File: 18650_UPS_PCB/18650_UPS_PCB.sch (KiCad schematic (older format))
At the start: 44 parts, among them J1 USB_B_Micro, J2 Conn_01x02, J3 Conn_01x02, SW1 SW_DIP_x02, U1 STLINK-V3MINI, U10 LR9102G-xx, U11 MP2667, U2 INA237, U3 EA_DOGS104N-A, U5 STM32L151RCTx

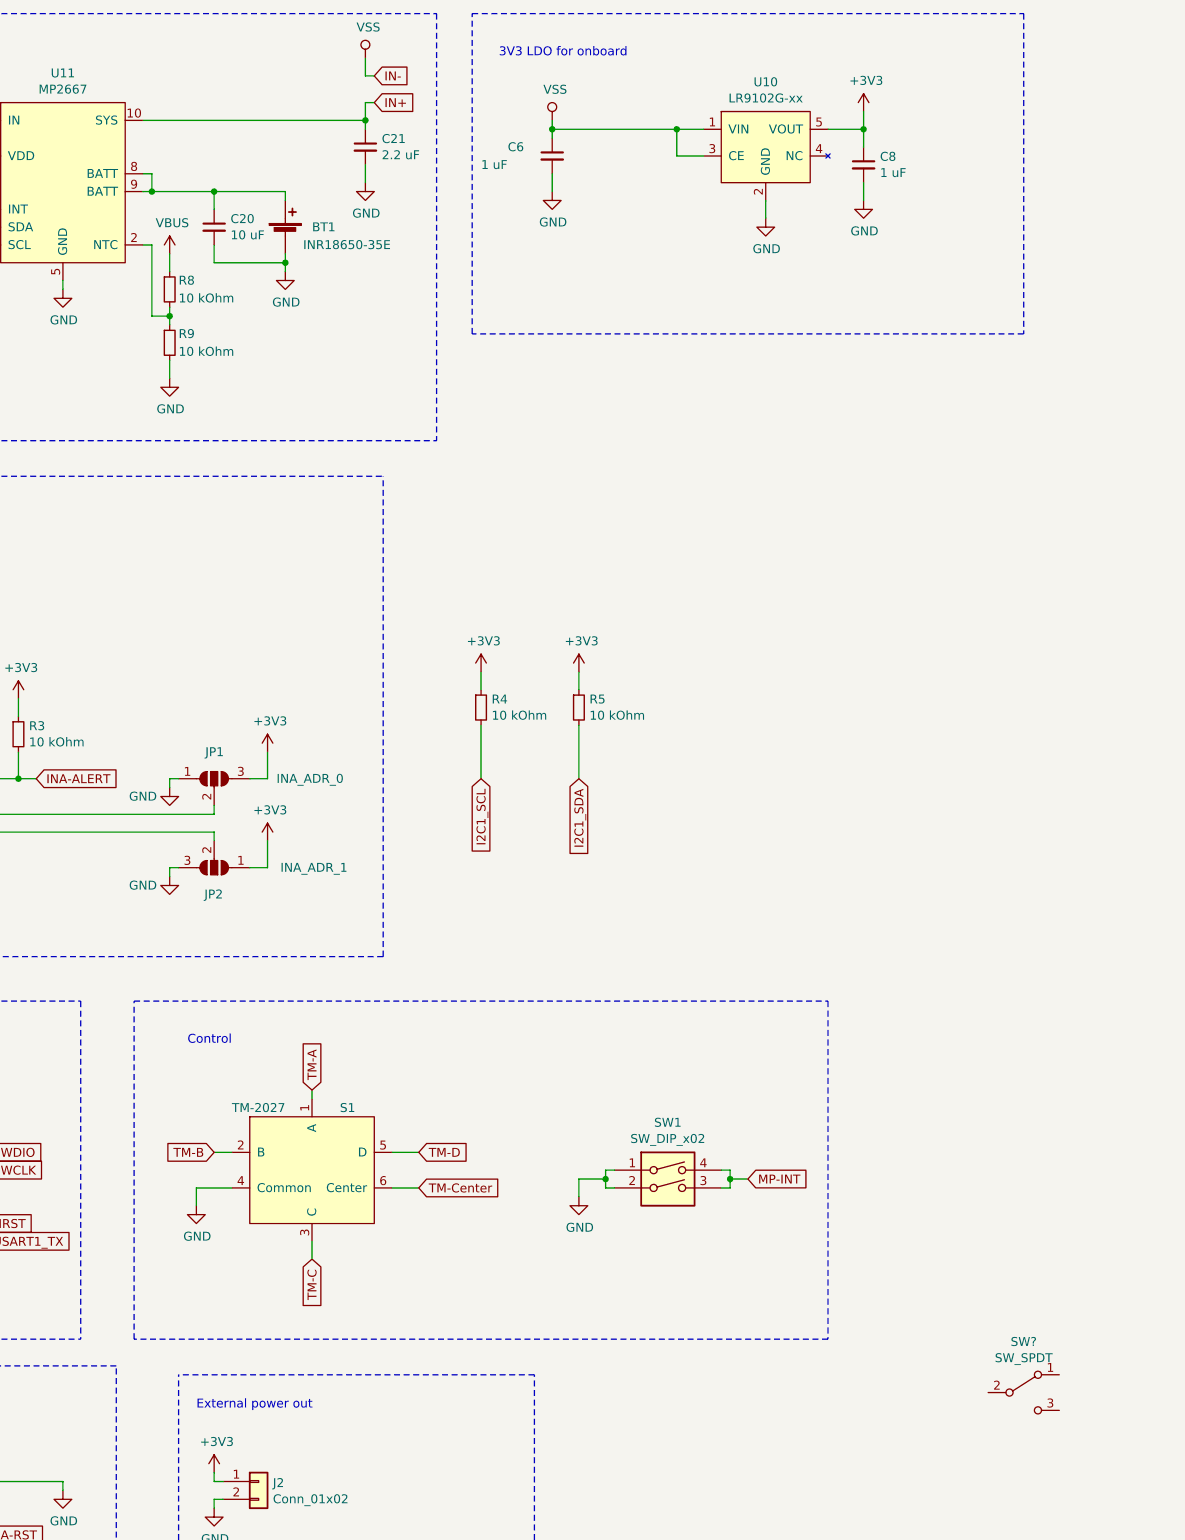
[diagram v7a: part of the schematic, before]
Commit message: added silkscreen markings
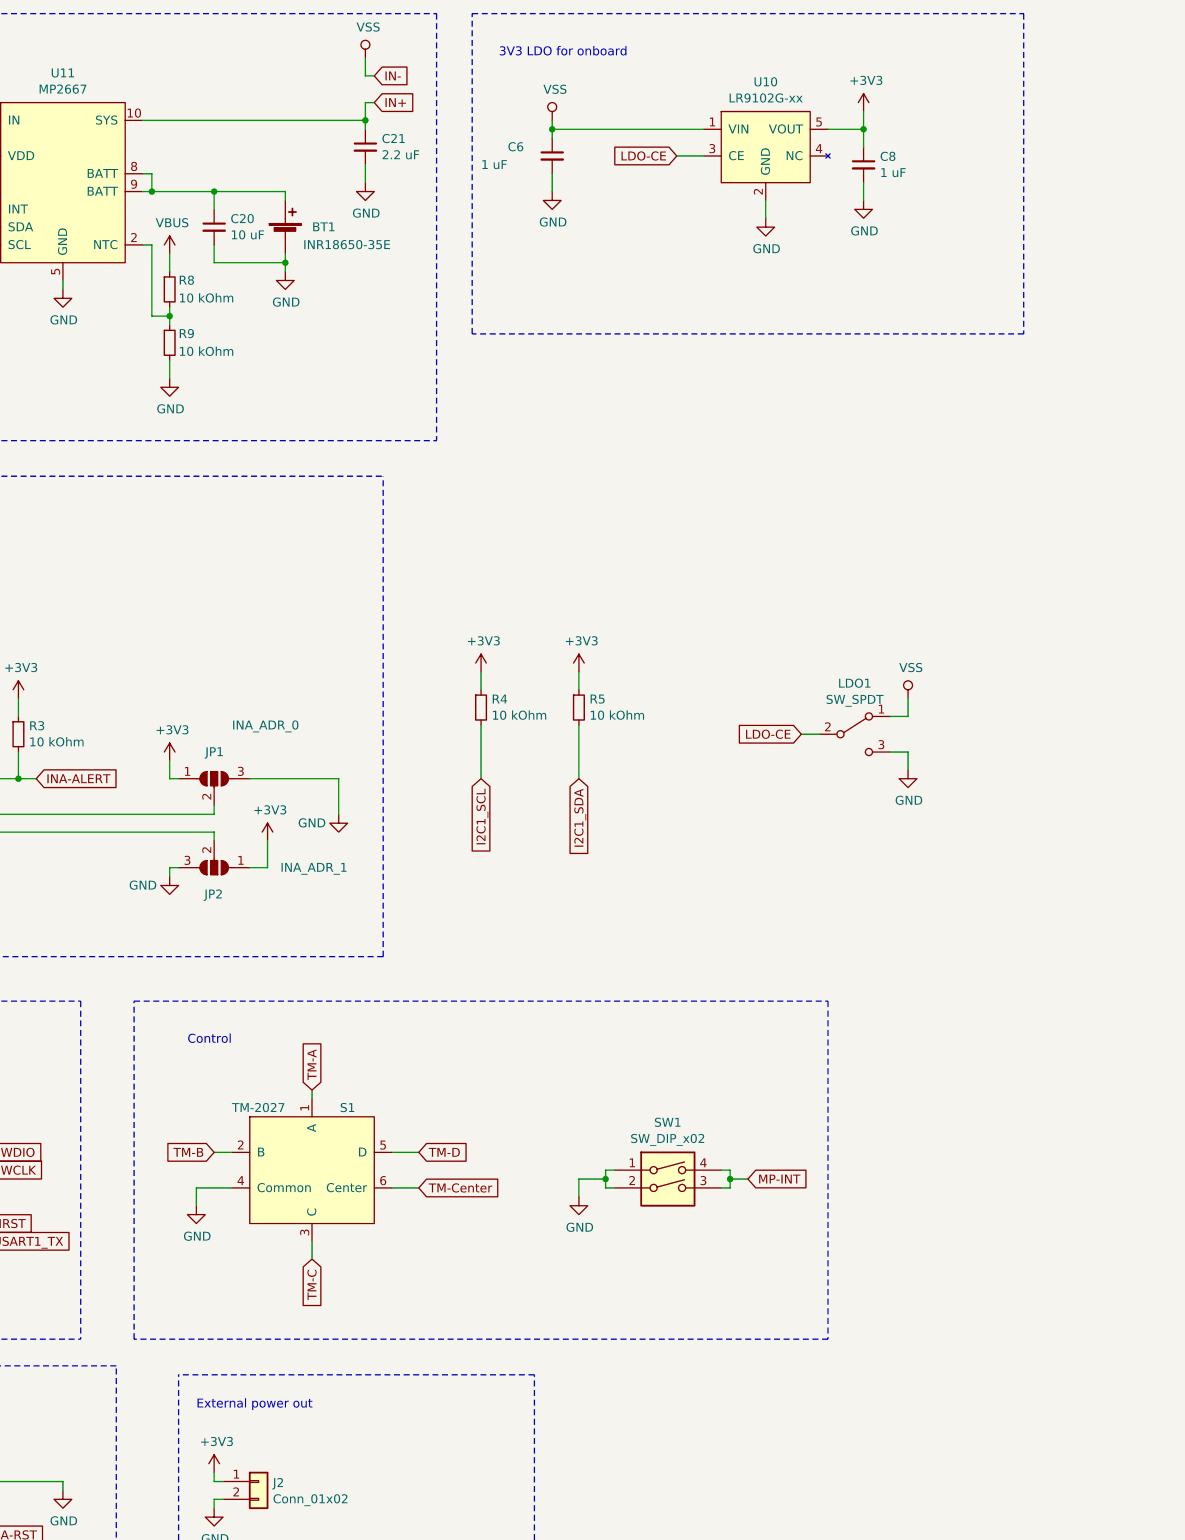
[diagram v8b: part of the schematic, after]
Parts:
- LDO1: renamed from SW?; footprint (none) -> Button_Switch_SMD:SW_SPDT_PCM12
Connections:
- net +3V3: now also JP1.1 (A); no longer JP1.3 (B)
- net GND: now also JP1.3 (B), LDO1.3 (C); no longer JP1.1 (A)
- net VSS: now also LDO1.1 (A); no longer U10.3 (CE)
- net LDO-CE: now reaches LDO1.2 (B)
- net LDO-CE: now also U10.3 (CE)
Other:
- moved on the sheet: LDO1
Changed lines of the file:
@@
 	5850 1300 5850 1250
-Wire Wire Line
-	5850 1300 6550 1300
 Wire Wire Line
 	6550 1450 6700 1450
@@
 P 3950 4950
 F 0 "JP1" H 3900 5100 50  0000 L CNN
-F 1 "INA_ADR_0" H 4300 4950 50  0000 L CNN
+F 1 "INA_ADR_0" H 4050 5250 50  0000 L CNN
 F 2 "Jumper:SolderJumper-3_P1.3mm_Open_RoundedPad1.0x1.5mm" H 3950 4950 50  0001 C CNN
 F 3 "~" H 3950 4950 50  0001 C CNN
@@
 	4150 5450 4250 5450
 Wire Wire Line
-	4150 4950 4250 4950
-Wire Wire Line
 	3950 5150 3950 5100
 Wire Wire Line
@@
 L power:GND #PWR0147
 U 1 1 620EFD95
-P 3700 5000
-F 0 "#PWR0147" H 3700 4750 50  0001 C CNN
-F 1 "GND" H 3550 4950 50  0000 C CNN
-F 2 "" H 3700 5000 50  0001 C CNN
-F 3 "" H 3700 5000 50  0001 C CNN
-	1    3700 5000
+P 4650 5150
+F 0 "#PWR0147" H 4650 4900 50  0001 C CNN
+F 1 "GND" H 4500 5100 50  0000 C CNN
+F 2 "" H 4650 5150 50  0001 C CNN
+F 3 "" H 4650 5150 50  0001 C CNN
+	1    4650 5150
 	1    0    0    -1
 $EndComp
@@
 Wire Wire Line
 	3700 5450 3750 5450
-Wire Wire Line
-	3700 5000 3700 4950
 Wire Wire Line
 	3700 4950 3750 4950
@@
 Wire Notes Line
 	3500 8100 3500 6200
-Wire Wire Line
-	6550 1450 6550 1300
-Connection ~ 6550 1300
-Wire Wire Line
-	6550 1300 6700 1300
 $Comp
 L power:+3V3 #PWR0126
@@
 L power:+3V3 #PWR0133
 U 1 1 6131FDDB
-P 4250 4800
-F 0 "#PWR0133" H 4250 4650 50  0001 C CNN
-F 1 "+3V3" H 4265 4973 50  0000 C CNN
-F 2 "" H 4250 4800 50  0001 C CNN
-F 3 "" H 4250 4800 50  0001 C CNN
-	1    4250 4800
+P 3700 4850
+F 0 "#PWR0133" H 3700 4700 50  0001 C CNN
+F 1 "+3V3" H 3715 5023 50  0000 C CNN
+F 2 "" H 3700 4850 50  0001 C CNN
+F 3 "" H 3700 4850 50  0001 C CNN
+	1    3700 4850
 	1    0    0    -1
 $EndComp
@@
 Wire Wire Line
 	4250 5450 4250 5300
-Wire Wire Line
-	4250 4950 4250 4800
 Wire Wire Line
 	2850 4600 2850 4500
@@
 NoConn ~ 14700 2250
 $Comp
-L Switch:SW_SPDT SW?
+L Switch:SW_SPDT LDO1
 U 1 1 614E8F27
-P 8500 8400
-F 0 "SW?" H 8500 8685 50  0000 C CNN
-F 1 "SW_SPDT" H 8500 8594 50  0000 C CNN
-F 2 "" H 8500 8400 50  0001 C CNN
-F 3 "~" H 8500 8400 50  0001 C CNN
-	1    8500 8400
-	1    0    0    -1
-$EndComp
+P 7550 4700
+F 0 "LDO1" H 7550 4985 50  0000 C CNN
+F 1 "SW_SPDT" H 7550 4894 50  0000 C CNN
+F 2 "Button_Switch_SMD:SW_SPDT_PCM12" H 7550 4700 50  0001 C CNN
+F 3 "~" H 7550 4700 50  0001 C CNN
+	1    7550 4700
+	1    0    0    -1
+$EndComp
+Text GLabel 6550 1450 0    50   Input ~ 0
+LDO-CE
+Wire Wire Line
+	5850 1300 6700 1300
+Text GLabel 7250 4700 0    50   Input ~ 0
+LDO-CE
+Wire Wire Line
+	7250 4700 7350 4700
+$Comp
+L power:GND #PWR0137
+U 1 1 610C0876
+P 7850 4900
+F 0 "#PWR0137" H 7850 4650 50  0001 C CNN
+F 1 "GND" H 7855 4727 50  0000 C CNN
+F 2 "" H 7850 4900 50  0001 C CNN
+F 3 "" H 7850 4900 50  0001 C CNN
+	1    7850 4900
+	1    0    0    -1
+$EndComp
+Wire Wire Line
+	7750 4800 7850 4800
+Wire Wire Line
+	7850 4800 7850 4900
+$Comp
+L power:VSS #PWR0138
+U 1 1 610CF4B9
+P 7850 4500
+F 0 "#PWR0138" H 7850 4350 50  0001 C CNN
+F 1 "VSS" H 7867 4673 50  0000 C CNN
+F 2 "" H 7850 4500 50  0001 C CNN
+F 3 "" H 7850 4500 50  0001 C CNN
+	1    7850 4500
+	1    0    0    -1
+$EndComp
+Wire Wire Line
+	7750 4600 7850 4600
+Wire Wire Line
+	7850 4600 7850 4500
+Wire Wire Line
+	3700 4950 3700 4850
+Wire Wire Line
+	4650 4950 4650 5150
+Wire Wire Line
+	4150 4950 4650 4950
 $EndSCHEMATC
